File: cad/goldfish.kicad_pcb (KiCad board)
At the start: 2 copper layers, 17.8 x 33 mm, 25 parts, among them J1 USB-C, J2 01x02, J3 01x12, J4 01x12, J5 01x05, U1 ATmega32U4, X1 16MHz

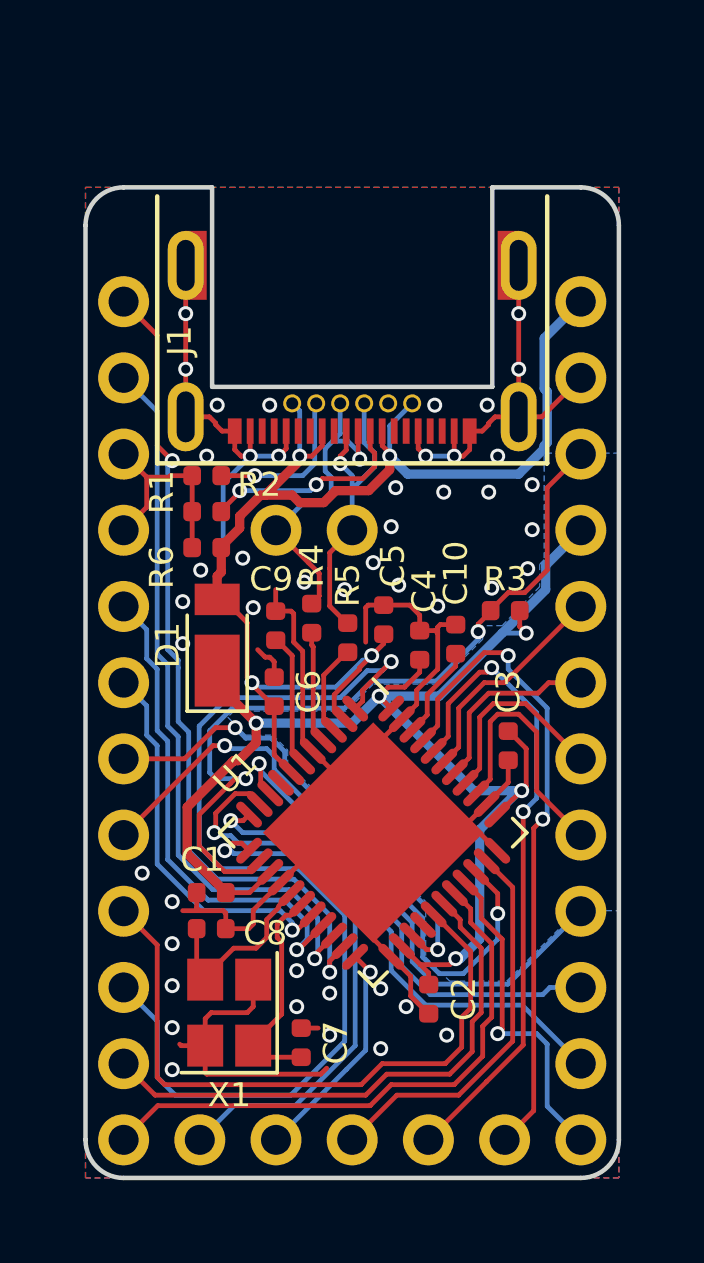
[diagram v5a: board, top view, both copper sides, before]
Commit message: Add initial V2 design
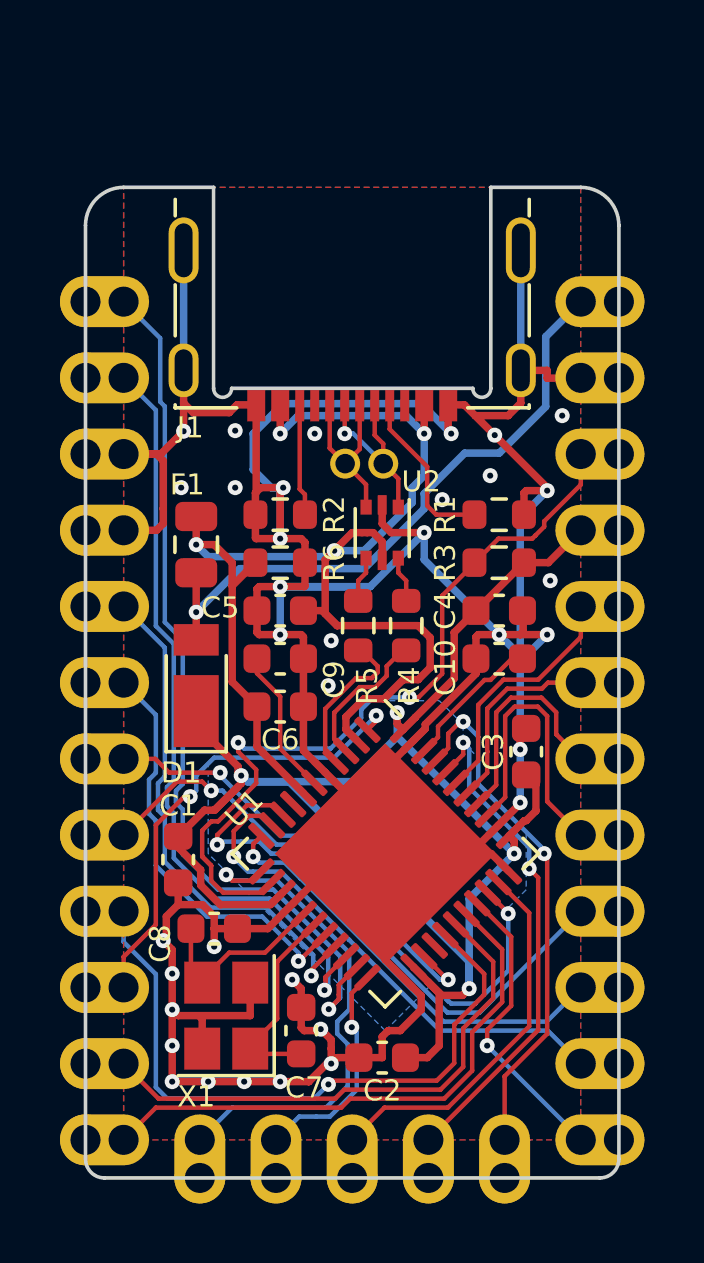
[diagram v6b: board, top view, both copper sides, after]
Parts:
- removed the G*** at (30.0, 43.8)
- added F1: 500mA, Fuse:Fuse_0805_2012Metric, F.Cu at (24.8, 35.4)
- added G***: LOGO, Goldfish Logo:Goldfish Silkscreen, B.Cu at (30.0, 42.0)
- added U2: USBLC6-2P6, Package_TO_SOT_SMD:SOT-666, F.Cu at (31.0, 35.0)
- C1, C10, C2, C3, C4, C5, C6, C7, C8, C9: footprint Capacitor_SMD:C_0402_1005Metric -> Capacitor_SMD:C_0603_1608Metric
- J1: value USB-C -> USB_C_Receptacle_USB2.0; footprint usb-type-c:CX70M-24P1 -> Molex 216990_GCT USB45xx_HRO TYPE-C-31-M-13x:Molex-216990_GCT-USB45xx_HRO-TYPE-C-31-M-13x
- J2: value 01x02 -> Conn_01x02; footprint pins:Pins2 -> Goldfish Pins:Pins_USB
- J3, J4: value 01x12 -> Conn_01x12; footprint pins:Pins12 -> Goldfish Pins:Pins_x12_Castellated
- J5: value 01x05 -> Conn_01x05; footprint pins:Pins5 -> Goldfish Pins:Pins_x05_Castellated
- R1, R2, R3, R4, R5, R6: footprint Resistor_SMD:R_0402_1005Metric -> Resistor_SMD:R_0603_1608Metric
- U1: value ATmega32U4 -> ATmega32U4-M
- moved R1 9.75 mm to (34.9, 34.4)
- moved C5 3.46 mm to (27.6, 37.6), turned to 180 degrees
- moved J2 3.20 mm to (29.8, 32.7)
- moved C4 2.89 mm to (34.9, 37.6), turned to 0 degrees
- moved R2 2.77 mm to (27.6, 34.4)
- moved R6 2.50 mm to (27.6, 36.0), turned to 180 degrees
- moved C2 2.49 mm to (31.0, 52.5), turned to 180 degrees
- moved R5 1.99 mm to (31.8, 38.1)
- moved R3 1.61 mm to (34.9, 36.0)
- moved C10 1.59 mm to (34.9, 39.2), turned to 180 degrees
- moved R4 1.57 mm to (30.2, 38.1), turned to -90 degrees
- moved C1 1.56 mm to (24.2, 45.9), turned to -90 degrees
- moved D1 1.52 mm to (24.8, 40.1)
- moved C9 1.11 mm to (27.6, 39.2), turned to 0 degrees
- moved U1 0.81 mm to (31.1, 45.7)
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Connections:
- net Net-(R5-Pad1) renamed /PD-
- D1 pad 2: VBUS -> /RAW
- J1 pad A8: Net-(J1-PadA8) -> unconnected-(J1-PadA8)
- J1 pad B8: Net-(J1-PadB8) -> unconnected-(J1-PadB8)
- J3 pad 1: VBUS -> /RAW
- R1 pad 1: GND -> Net-(J1-PadA5)
- R1 pad 2: Net-(J1-PadA5) -> GND
- R4 pad 2: /D+ -> /PD+
- R5 pad 2: /D- -> Net-(R5-Pad2)
- U1 pad 26: Net-(U1-Pad26) -> unconnected-(U1-Pad26)
- U1 pad 4: Net-(R4-Pad1) -> /PD+
- U1 pad 8: Net-(U1-Pad8) -> unconnected-(U1-Pad8)
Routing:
- net GND: track 94.6 -> 160.1 mm, vias 46 -> 35
- net /RAW: track 0.00 -> 21.0 mm, vias 0 -> 1
- net /PE6: track 34.1 -> 15.6 mm, vias 1 -> 2
- net VCC: track 49.8 -> 59.6 mm, vias 5 -> 4
- net /PD+: track 0.00 -> 5.23 mm
- net /D+: track 11.0 -> 6.07 mm, vias 1 -> 0
- net /PF1: track 21.6 -> 17.0 mm
- net /PF0: track 21.9 -> 17.5 mm
- net /D-: track 10.5 -> 6.40 mm
- net Net-(R4-Pad1): track 3.75 -> 1.53 mm
- net /PB1: track 16.8 -> 19.0 mm
- net /PD3: track 27.9 -> 29.8 mm, vias 2 -> 1
- net /PB2: track 18.7 -> 16.9 mm
- net /PD-: track 3.08 -> 4.89 mm
- net Net-(C10-Pad1): track 3.13 -> 4.76 mm
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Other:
- outline, holes or cut-outs redrawn
- board text added: "v2 rev0"
- board text removed: "Rev.D"

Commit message: Adjust USB-C connector 3D model position
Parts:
- G***: footprint Goldfish Logo:Goldfish Silkscreen -> Goldfish Logo:Goldfish_Silkscreen

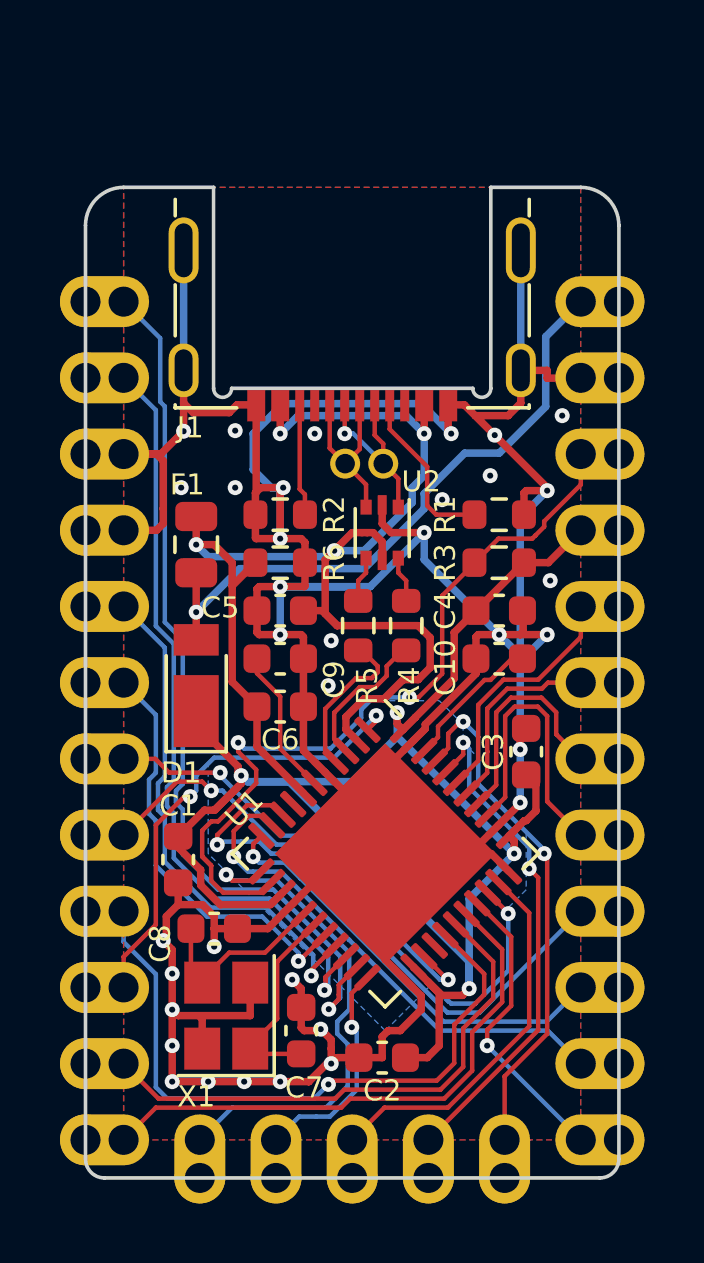
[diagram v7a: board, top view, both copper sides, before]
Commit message: Switch D1 to SOD 123F
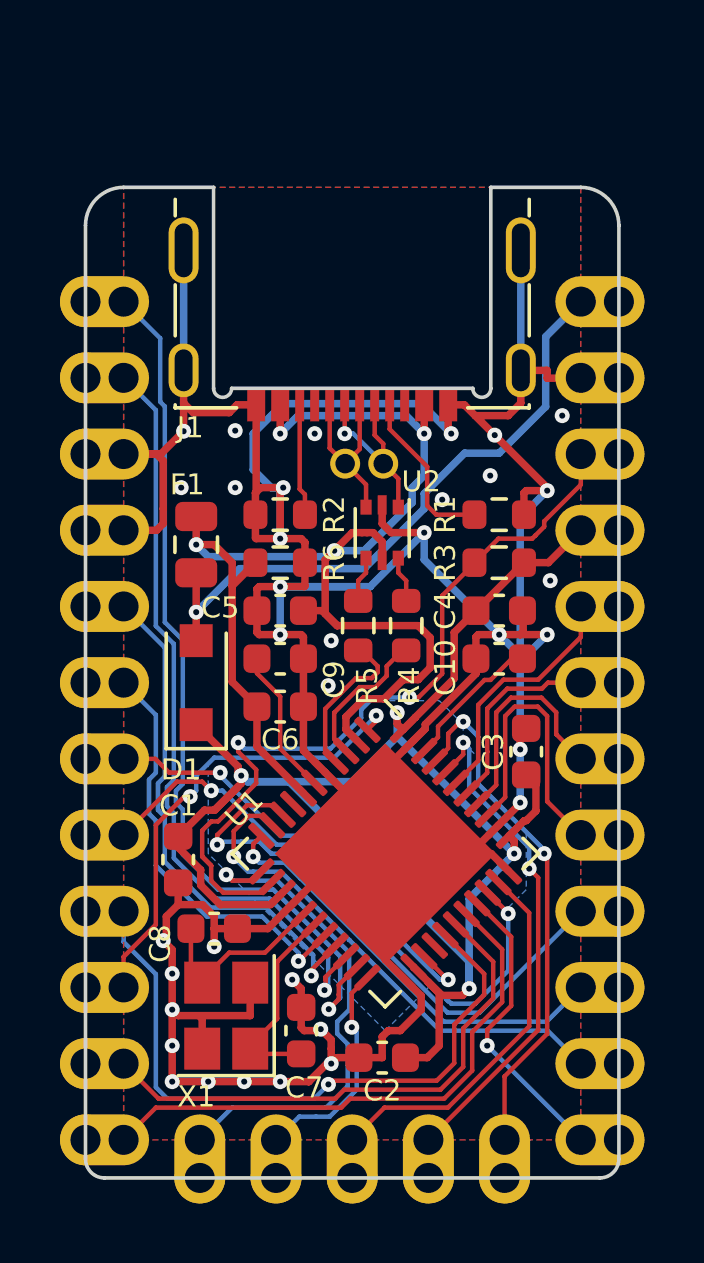
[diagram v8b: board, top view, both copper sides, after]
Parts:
- D1: footprint Diode_SMD:D_PowerDI-123 -> Diode_SMD:D_SOD-123F
- moved D1 0.10 mm to (24.8, 40.0)
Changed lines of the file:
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@@
     )
   )
-  (footprint "Diode_SMD:D_PowerDI-123" (layer "F.Cu")
-    (at 24.8 40.1 90)
-    (descr "http://www.diodes.com/_files/datasheets/ds30497.pdf")
-    (tags "PowerDI diode vishay")
+  (footprint "Diode_SMD:D_SOD-123F" (layer "F.Cu")
+    (at 24.8 40 90)
+    (descr "D_SOD-123F")
+    (tags "D_SOD-123F")
     (property "Sheetfile" "goldfish.kicad_sch")
     (property "Sheetname" "")
@@
       (effects (font (size 0.7 0.7) (thickness 0.125)))
     )
-    (fp_text value "D_Schottky" (at 0 2.5 90) (layer "F.Fab")
+    (fp_text value "D_Schottky" (at 0 2.1 90) (layer "F.Fab")
       (effects (font (size 1 1) (thickness 0.15)))
     )
-    (fp_text user "${REFERENCE}" (at 0 -2 90) (layer "F.Fab")
-      (effects (font (size 0.7 0.7) (thickness 0.125)))
+    (fp_text user "${REFERENCE}" (at -0.127 -1.905 90) (layer "F.Fab")
+      (effects (font (size 1 1) (thickness 0.15)))
     )
-    (fp_line (start 1 -1) (end -2.2 -1) (layer "F.SilkS") (width 0.12))
-    (fp_line (start -2.2 1) (end -2.2 -1) (layer "F.SilkS") (width 0.12))
-    (fp_line (start -2.2 1) (end 1 1) (layer "F.SilkS") (width 0.12))
-    (fp_line (start -2.5 1.3) (end -2.5 -1.3) (layer "F.CrtYd") (width 0.05))
-    (fp_line (start 2.5 -1.3) (end 2.5 1.3) (layer "F.CrtYd") (width 0.05))
-    (fp_line (start -2.5 -1.3) (end 2.5 -1.3) (layer "F.CrtYd") (width 0.05))
-    (fp_line (start 2.5 1.3) (end -2.5 1.3) (layer "F.CrtYd") (width 0.05))
-    (fp_line (start 1.4 0.9) (end -1.4 0.9) (layer "F.Fab") (width 0.1))
-    (fp_line (start -1.4 0.9) (end -1.4 -0.9) (layer "F.Fab") (width 0.1))
-    (fp_line (start 0.3 0) (end 0.7 0) (layer "F.Fab") (width 0.1))
-    (fp_line (start -0.8 0) (end -0.5 0) (layer "F.Fab") (width 0.1))
-    (fp_line (start -0.5 0) (end -0.5 0.5) (layer "F.Fab") (width 0.1))
-    (fp_line (start 0.3 -0.5) (end -0.5 0) (layer "F.Fab") (width 0.1))
-    (fp_line (start -1.4 -0.9) (end 1.4 -0.9) (layer "F.Fab") (width 0.1))
-    (fp_line (start -0.5 0) (end -0.5 -0.5) (layer "F.Fab") (width 0.1))
-    (fp_line (start 0.3 0.5) (end 0.3 -0.5) (layer "F.Fab") (width 0.1))
-    (fp_line (start -0.5 0) (end 0.3 0.5) (layer "F.Fab") (width 0.1))
+    (fp_line (start -2.2 -1) (end 1.65 -1) (layer "F.SilkS") (width 0.12))
+    (fp_line (start -2.2 -1) (end -2.2 1) (layer "F.SilkS") (width 0.12))
+    (fp_line (start -2.2 1) (end 1.65 1) (layer "F.SilkS") (width 0.12))
+    (fp_line (start -2.2 -1.15) (end -2.2 1.15) (layer "F.CrtYd") (width 0.05))
+    (fp_line (start 2.2 -1.15) (end 2.2 1.15) (layer "F.CrtYd") (width 0.05))
+    (fp_line (start -2.2 -1.15) (end 2.2 -1.15) (layer "F.CrtYd") (width 0.05))
+    (fp_line (start 2.2 1.15) (end -2.2 1.15) (layer "F.CrtYd") (width 0.05))
+    (fp_line (start 0.25 -0.4) (end 0.25 0.4) (layer "F.Fab") (width 0.1))
+    (fp_line (start -0.75 0) (end -0.35 0) (layer "F.Fab") (width 0.1))
+    (fp_line (start -0.35 0) (end 0.25 -0.4) (layer "F.Fab") (width 0.1))
+    (fp_line (start -0.35 0) (end -0.35 0.55) (layer "F.Fab") (width 0.1))
     (fp_line (start 1.4 -0.9) (end 1.4 0.9) (layer "F.Fab") (width 0.1))
-    (pad "1" smd rect (at -0.85 0 270) (size 2.4 1.5) (layers "F.Cu" "F.Paste" "F.Mask")
+    (fp_line (start 0.25 0.4) (end -0.35 0) (layer "F.Fab") (width 0.1))
+    (fp_line (start -0.35 0) (end -0.35 -0.55) (layer "F.Fab") (width 0.1))
+    (fp_line (start -1.4 -0.9) (end 1.4 -0.9) (layer "F.Fab") (width 0.1))
+    (fp_line (start -1.4 0.9) (end -1.4 -0.9) (layer "F.Fab") (width 0.1))
+    (fp_line (start 0.25 0) (end 0.75 0) (layer "F.Fab") (width 0.1))
+    (fp_line (start 1.4 0.9) (end -1.4 0.9) (layer "F.Fab") (width 0.1))
+    (pad "1" smd rect (at -1.4 0 90) (size 1.1 1.1) (layers "F.Cu" "F.Paste" "F.Mask")
       (net 1 "VCC") (pinfunction "K") (pintype "passive"))
-    (pad "2" smd rect (at 1.525 0 270) (size 1.05 1.5) (layers "F.Cu" "F.Paste" "F.Mask")
+    (pad "2" smd rect (at 1.4 0 90) (size 1.1 1.1) (layers "F.Cu" "F.Paste" "F.Mask")
       (net 44 "/RAW") (pinfunction "A") (pintype "passive"))
-    (model "${KICAD6_3DMODEL_DIR}/Diode_SMD.3dshapes/D_PowerDI-123.wrl"
+    (model "${KICAD6_3DMODEL_DIR}/Diode_SMD.3dshapes/D_SOD-123F.wrl"
       (offset (xyz 0 0 0))
       (scale (xyz 1 1 1))
@@
   (segment (start 36.54 36) (end 37.62 34.92) (width 0.25) (layer "F.Cu") (net 1))
   (segment (start 32.982739 50.424511) (end 33.675489 50.424511) (width 0.25) (layer "F.Cu") (net 1))
+  (segment (start 26.2 42.8) (end 24.8 41.4) (width 0.25) (layer "F.Cu") (net 1))
   (segment (start 35.4 45.280062) (end 35.4 45.7) (width 0.25) (layer "F.Cu") (net 1))
   (segment (start 34.125 37.6) (end 35.725 36) (width 0.25) (layer "F.Cu") (net 1))
@@
   (segment (start 35.735534 44.6) (end 35.8 44.6) (width 0.25) (layer "F.Cu") (net 1))
   (segment (start 31.775 52.5) (end 32.5 52.5) (width 0.25) (layer "F.Cu") (net 1))
-  (segment (start 24.8 41.4) (end 26.2 42.8) (width 0.25) (layer "F.Cu") (net 1))
   (segment (start 31.692202 41.572264) (end 31.5 41.380062) (width 0.25) (layer "F.Cu") (net 1))
   (segment (start 24.94952 46.74952) (end 24.94952 46.243093) (width 0.25) (layer "F.Cu") (net 1))
@@
   (segment (start 35.725 36) (end 36.54 36) (width 0.25) (layer "F.Cu") (net 1))
   (segment (start 35.227736 45.107798) (end 35.4 45.280062) (width 0.25) (layer "F.Cu") (net 1))
-  (segment (start 24.8 40.95) (end 24.8 41.4) (width 0.25) (layer "F.Cu") (net 1))
   (segment (start 26.3 43.1) (end 26.3 43.360935) (width 0.25) (layer "F.Cu") (net 1))
   (segment (start 32.1 41.16064) (end 32.1 41.164466) (width 0.25) (layer "F.Cu") (net 1))
@@
   (segment (start 31.5375 35.85) (end 31.5375 36.3375) (width 0.15) (layer "F.Cu") (net 43))
   (segment (start 31.5375 36.3375) (end 31.8 36.6) (width 0.15) (layer "F.Cu") (net 43))
+  (segment (start 24.8 37.65) (end 24.8 38.6) (width 0.25) (layer "F.Cu") (net 44))
   (segment (start 24.8 36.3375) (end 24.8 37.65) (width 0.25) (layer "F.Cu") (net 44))
-  (segment (start 24.8 37.65) (end 24.8 38.575) (width 0.25) (layer "F.Cu") (net 44))
   (via (at 24.8 37.65) (size 0.5) (drill 0.2) (layers "F.Cu" "B.Cu") (net 44))
   (segment (start 32.4 33.7) (end 33.75 32.35) (width 0.25) (layer "B.Cu") (net 44))
